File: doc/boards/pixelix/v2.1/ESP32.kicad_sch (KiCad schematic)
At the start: 2 parts, among them U1 ESP32-DEVKITC-32D

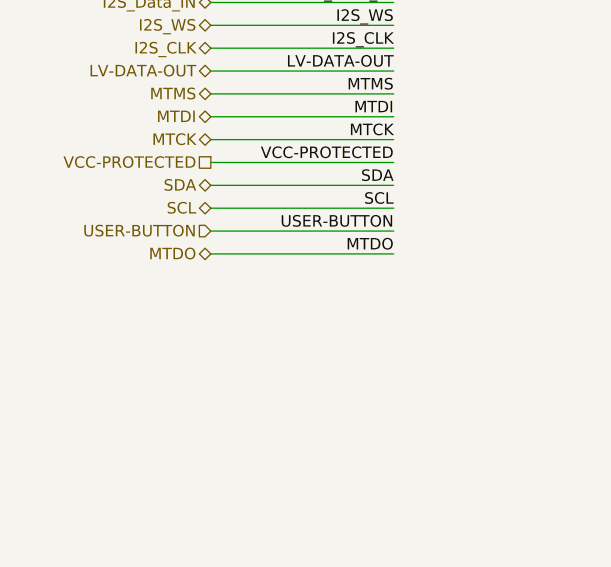
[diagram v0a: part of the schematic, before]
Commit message: #91 HW v2.1: - One Wire added (see #40) - 3V3 and GND to I2S, I2C and One-Wire interface added - Testpoint added
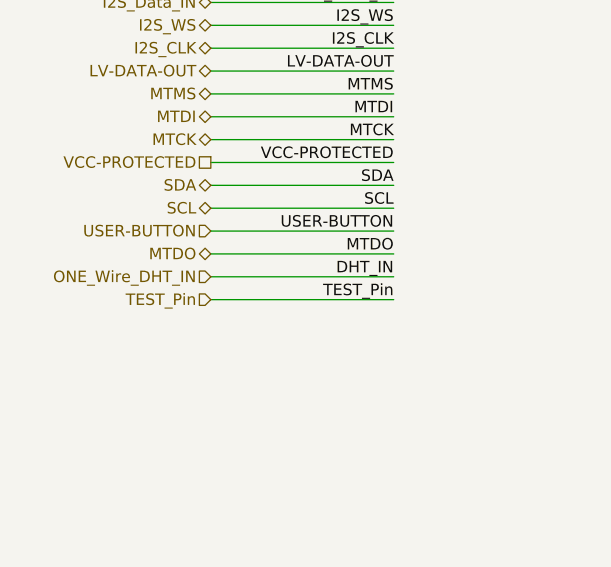
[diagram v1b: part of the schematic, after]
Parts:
- A1: footprint Module:Adafruit_Feather -> footprints:Adafruit_Feather_V2_ESP32
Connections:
- net DHT_IN renamed ONE_Wire_DHT_IN
